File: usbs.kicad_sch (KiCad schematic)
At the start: 34 parts, among them J2 USB-A_Amphenol_UE27AC54100, J3 USB-C_GCT_USB4105-GF-A, J4 USB-C_GCT_USB4105-GF-A, U3 FT4232H_VQFN, Y1 Resonator_12MHz_ABM8G

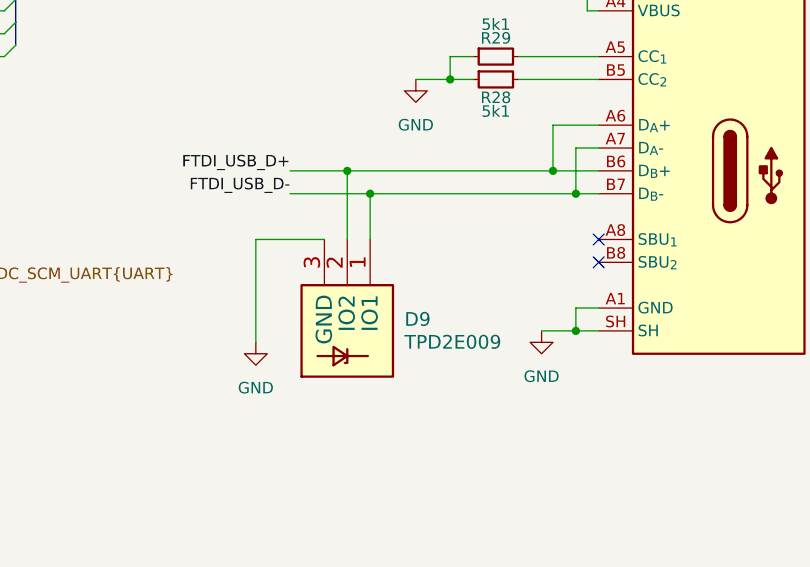
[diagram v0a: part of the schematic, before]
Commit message: [#92504] Remove TVS diodes from debug USB
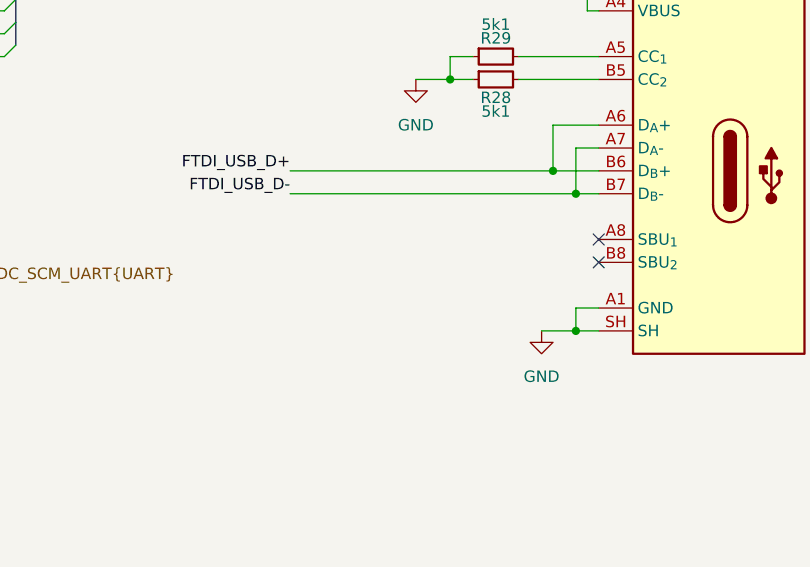
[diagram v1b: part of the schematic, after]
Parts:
- removed D9: TPD2E009, bmc-breakout-board-footprints:SOT-3, symbol bmc-breakout-board:TPD2E009

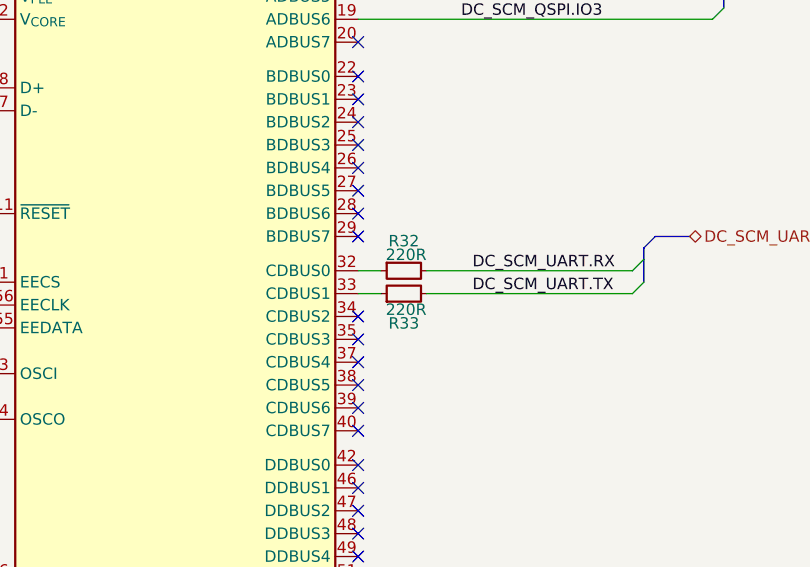
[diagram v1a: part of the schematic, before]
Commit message: [#92504] Change USART resistors to 100 Ohm
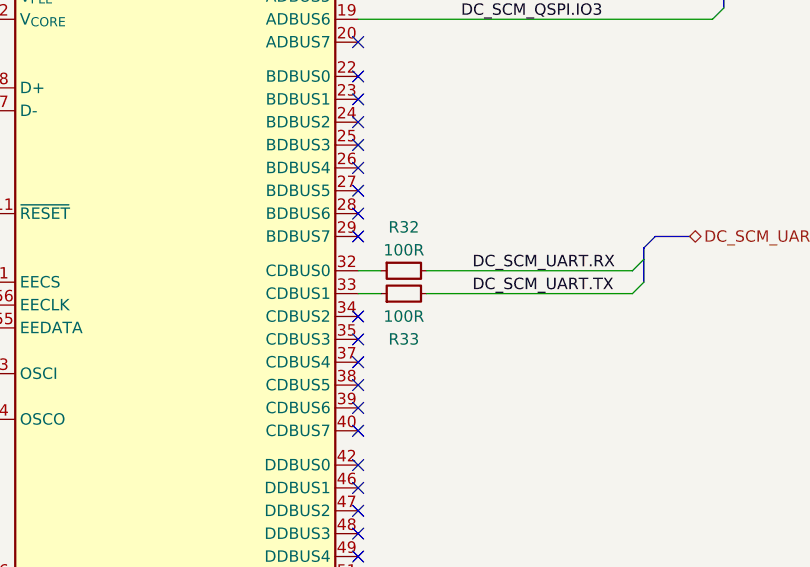
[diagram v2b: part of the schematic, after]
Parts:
- removed R32, R33: R_220R_0402, antmicro-footprints:R_0402_1005Metric, symbol antmicroResistors0402:R_220R_0402
- added R32, R33: R_100R_0402, antmicro-footprints:R_0402_1005Metric, symbol antmicroResistors0402:R_100R_0402
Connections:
- net DC_SCM_UART.RX: now also R32.2
- net DC_SCM_UART.TX: now also R33.2
- net at U3.33 (CDBUS1): now also R33.1
- net at U3.32 (CDBUS0): now also R32.1

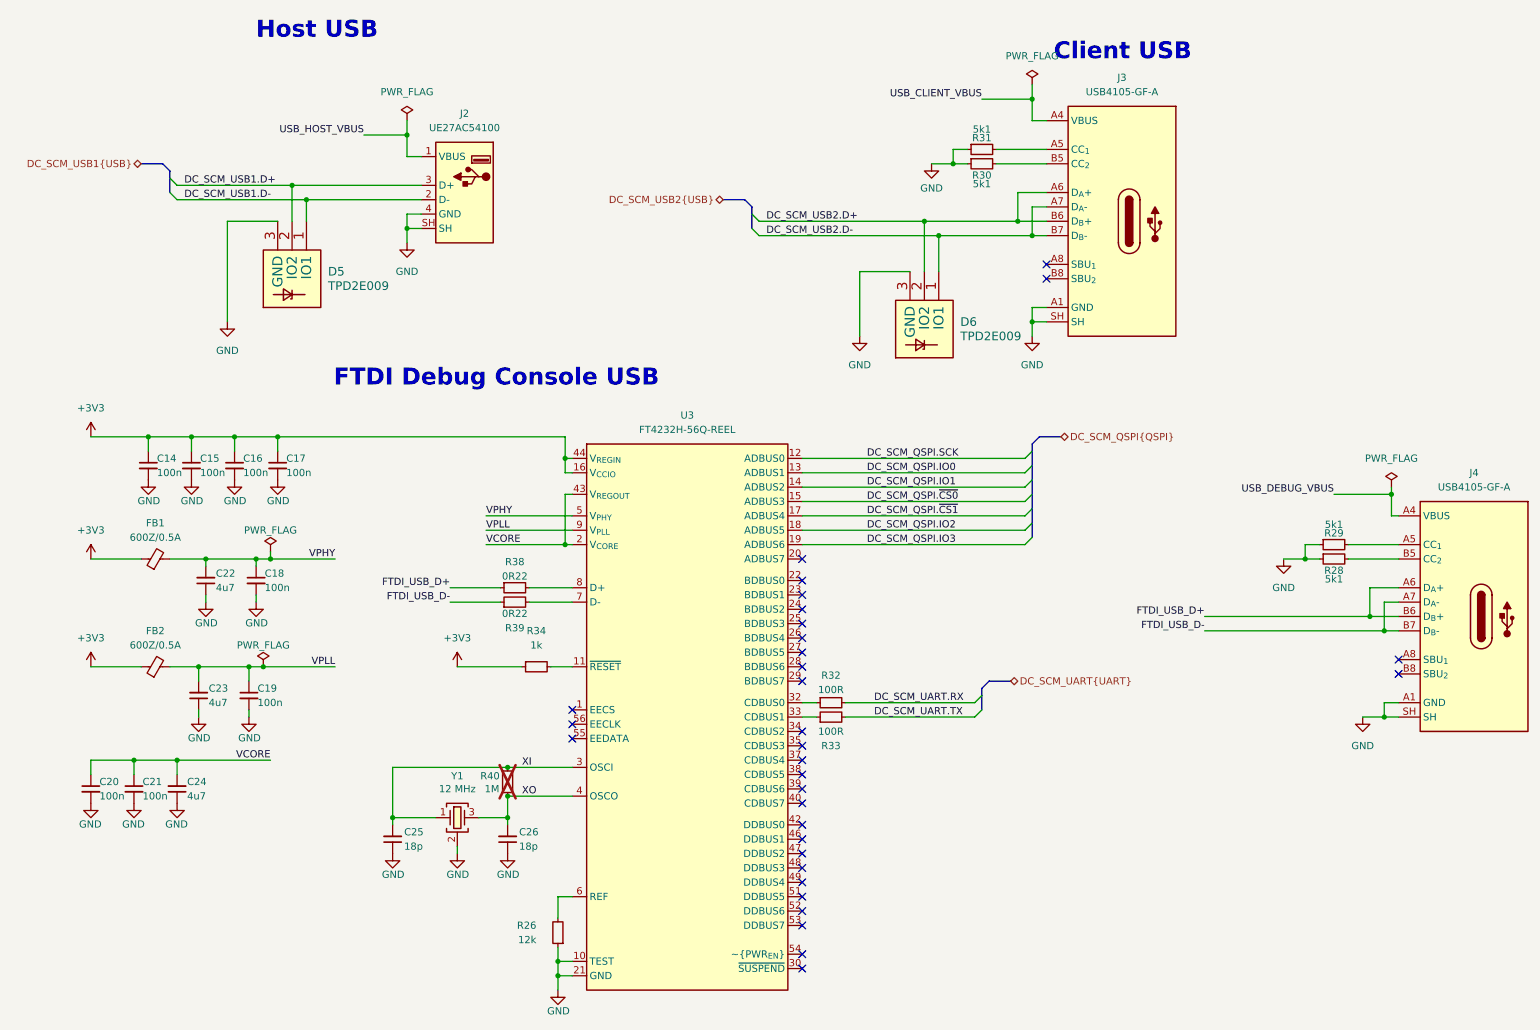
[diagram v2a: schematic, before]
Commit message: [#93090] Add FTDI LDO
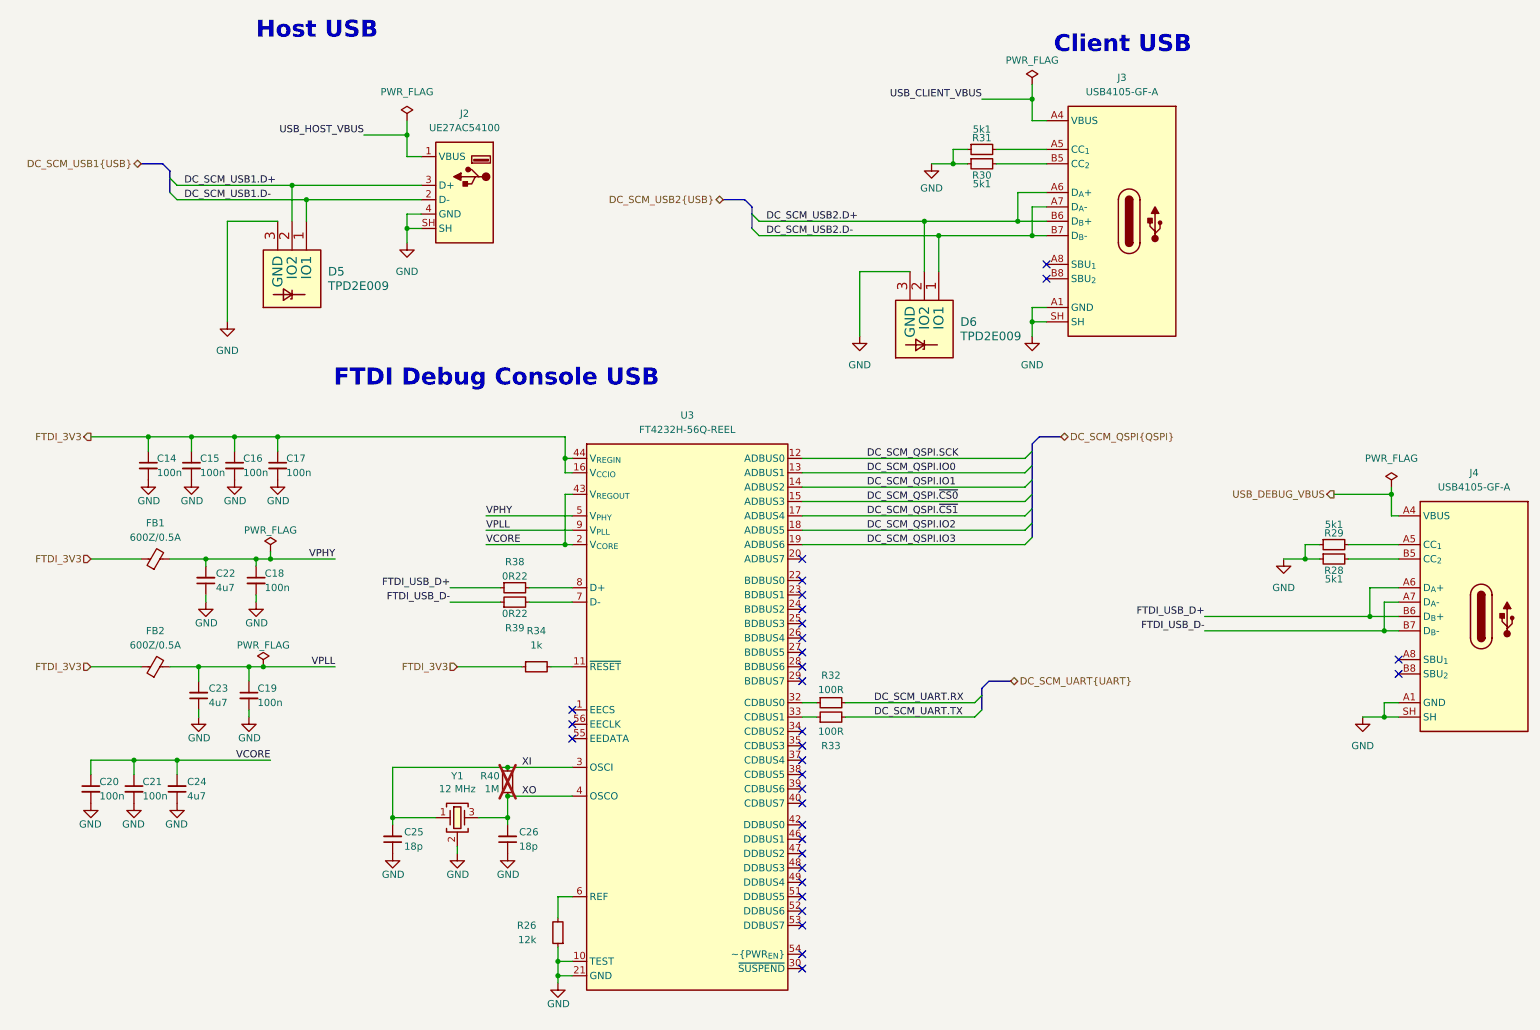
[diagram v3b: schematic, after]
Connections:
- net +3V3 renamed FTDI_3V3

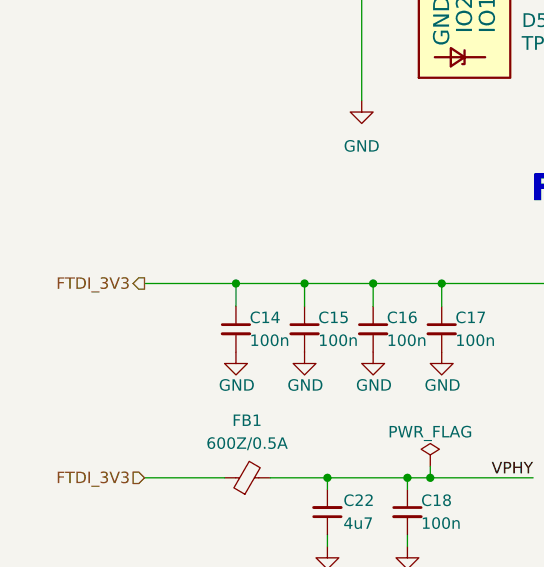
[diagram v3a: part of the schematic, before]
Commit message: [#93090] Change Antmicro Logo and finish 3V3 FTDI power schematic
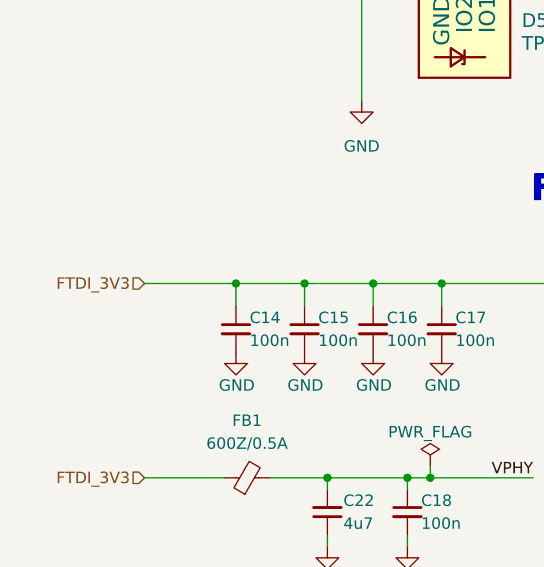
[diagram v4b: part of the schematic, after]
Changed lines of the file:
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@@
 	)
 	(hierarchical_label "FTDI_3V3"
-		(shape output)
+		(shape input)
 		(at 26.67 96.52 180)
 		(effects
